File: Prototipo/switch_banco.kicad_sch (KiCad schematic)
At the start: 9 parts, among them Q1_1 MMBT2222A, Q1_2 MMBFJ201

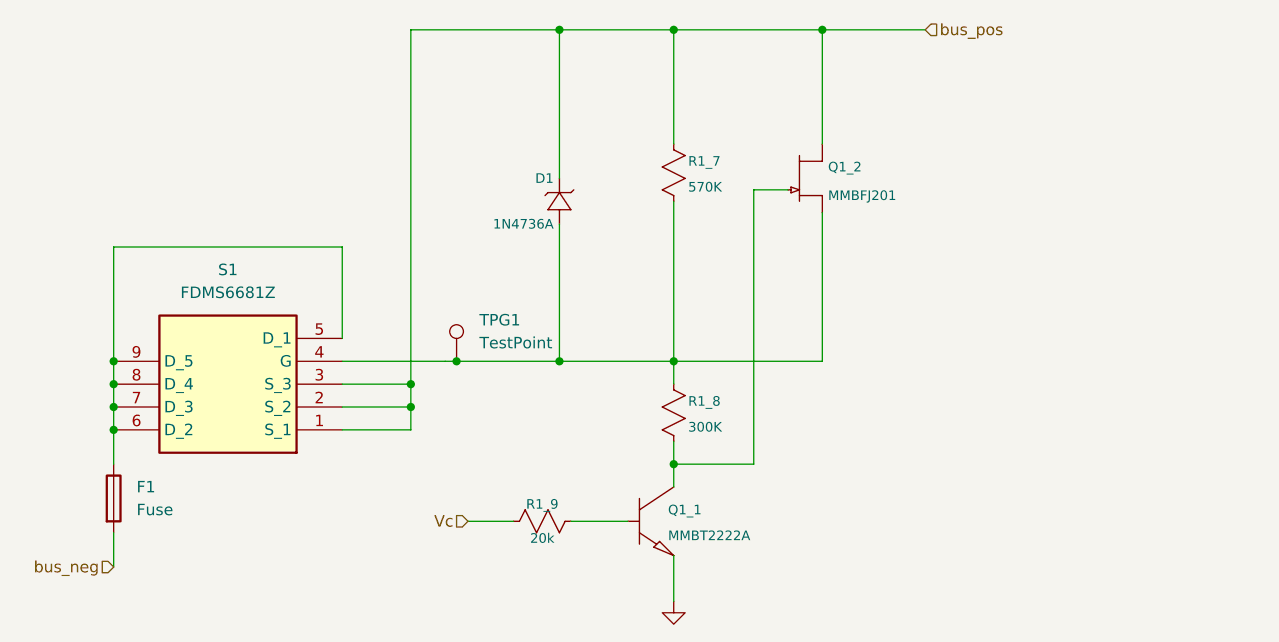
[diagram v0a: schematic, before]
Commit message: Suma leds a kicad, falta rutear
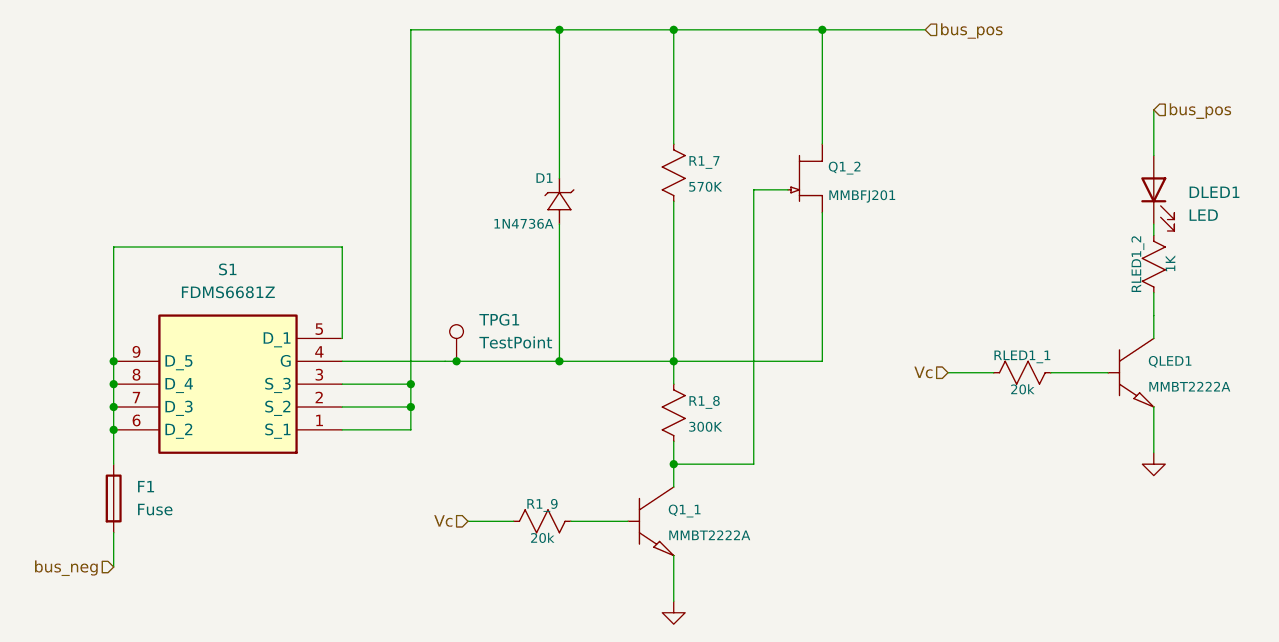
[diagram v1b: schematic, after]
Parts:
- added DLED1: LED, LED_THT:LED_D5.0mm, symbol Device:LED
- added QLED1: MMBT2222A, Package_TO_SOT_SMD:SOT-23-3, symbol modificados:npn
- added RLED1_1: 20k, Resistor_THT:R_Axial_DIN0207_L6.3mm_D2.5mm_P7.62mm_Horizontal, symbol ltspice:res
- added RLED1_2: 1K, Resistor_THT:R_Axial_DIN0207_L6.3mm_D2.5mm_P7.62mm_Horizontal, symbol ltspice:res
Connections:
- net 0: now also QLED1.2 (E)
- net Vc: now also RLED1_1.2
- net bus_pos: now also DLED1.2 (A)
- new net: QLED1.1 (B), RLED1_1.1
- new net: QLED1.3 (C), RLED1_2.2
- new net: DLED1.1 (K), RLED1_2.1

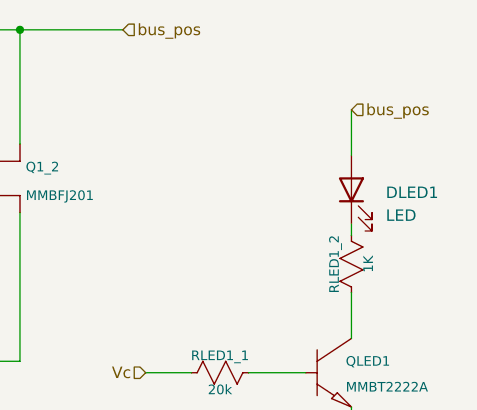
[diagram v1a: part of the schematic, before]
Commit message: se suman los leds al pcb
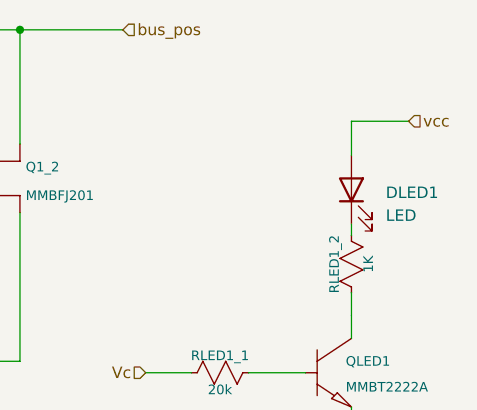
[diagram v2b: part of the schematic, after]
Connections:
- net bus_pos: no longer DLED1.2 (A)
- new net vcc: DLED1.2 (A)
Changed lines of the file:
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@@
+	(wire
+		(pts
+			(xy 185.42 63.5) (xy 179.07 63.5)
+		)
+		(stroke
+			(width 0)
+			(type default)
+		)
+	)
 	(wire
 		(pts
@@
 	(wire
 		(pts
+			(xy 179.07 63.5) (xy 179.07 67.31)
+		)
+		(stroke
+			(width 0)
+			(type default)
+		)
+	)
+	(wire
+		(pts
 			(xy 113.03 69.85) (xy 113.03 53.34)
 		)
@@
 	(wire
 		(pts
-			(xy 179.07 62.23) (xy 179.07 67.31)
-		)
-		(stroke
-			(width 0)
-			(type default)
-		)
-	)
-	(wire
-		(pts
 			(xy 173.99 91.44) (xy 167.64 91.44)
 		)
@@
 			(width 0.1524)
 			(type solid)
-		)
-	)
-	(hierarchical_label "bus_pos"
-		(shape input)
-		(at 179.07 62.23 0)
-		(effects
-			(font
-				(size 1.27 1.27)
-			)
-			(justify left)
 		)
 	)
@@
 		(effects
 			(font
+				(size 1.27 1.27)
+			)
+			(justify left)
+		)
+	)
+	(hierarchical_label "vcc"
+		(shape input)
+		(at 185.42 63.5 0)
+		(effects
+			(font
